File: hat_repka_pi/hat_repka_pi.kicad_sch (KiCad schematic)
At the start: 6 parts, among them J1 GPIO, U1 CAT24C256

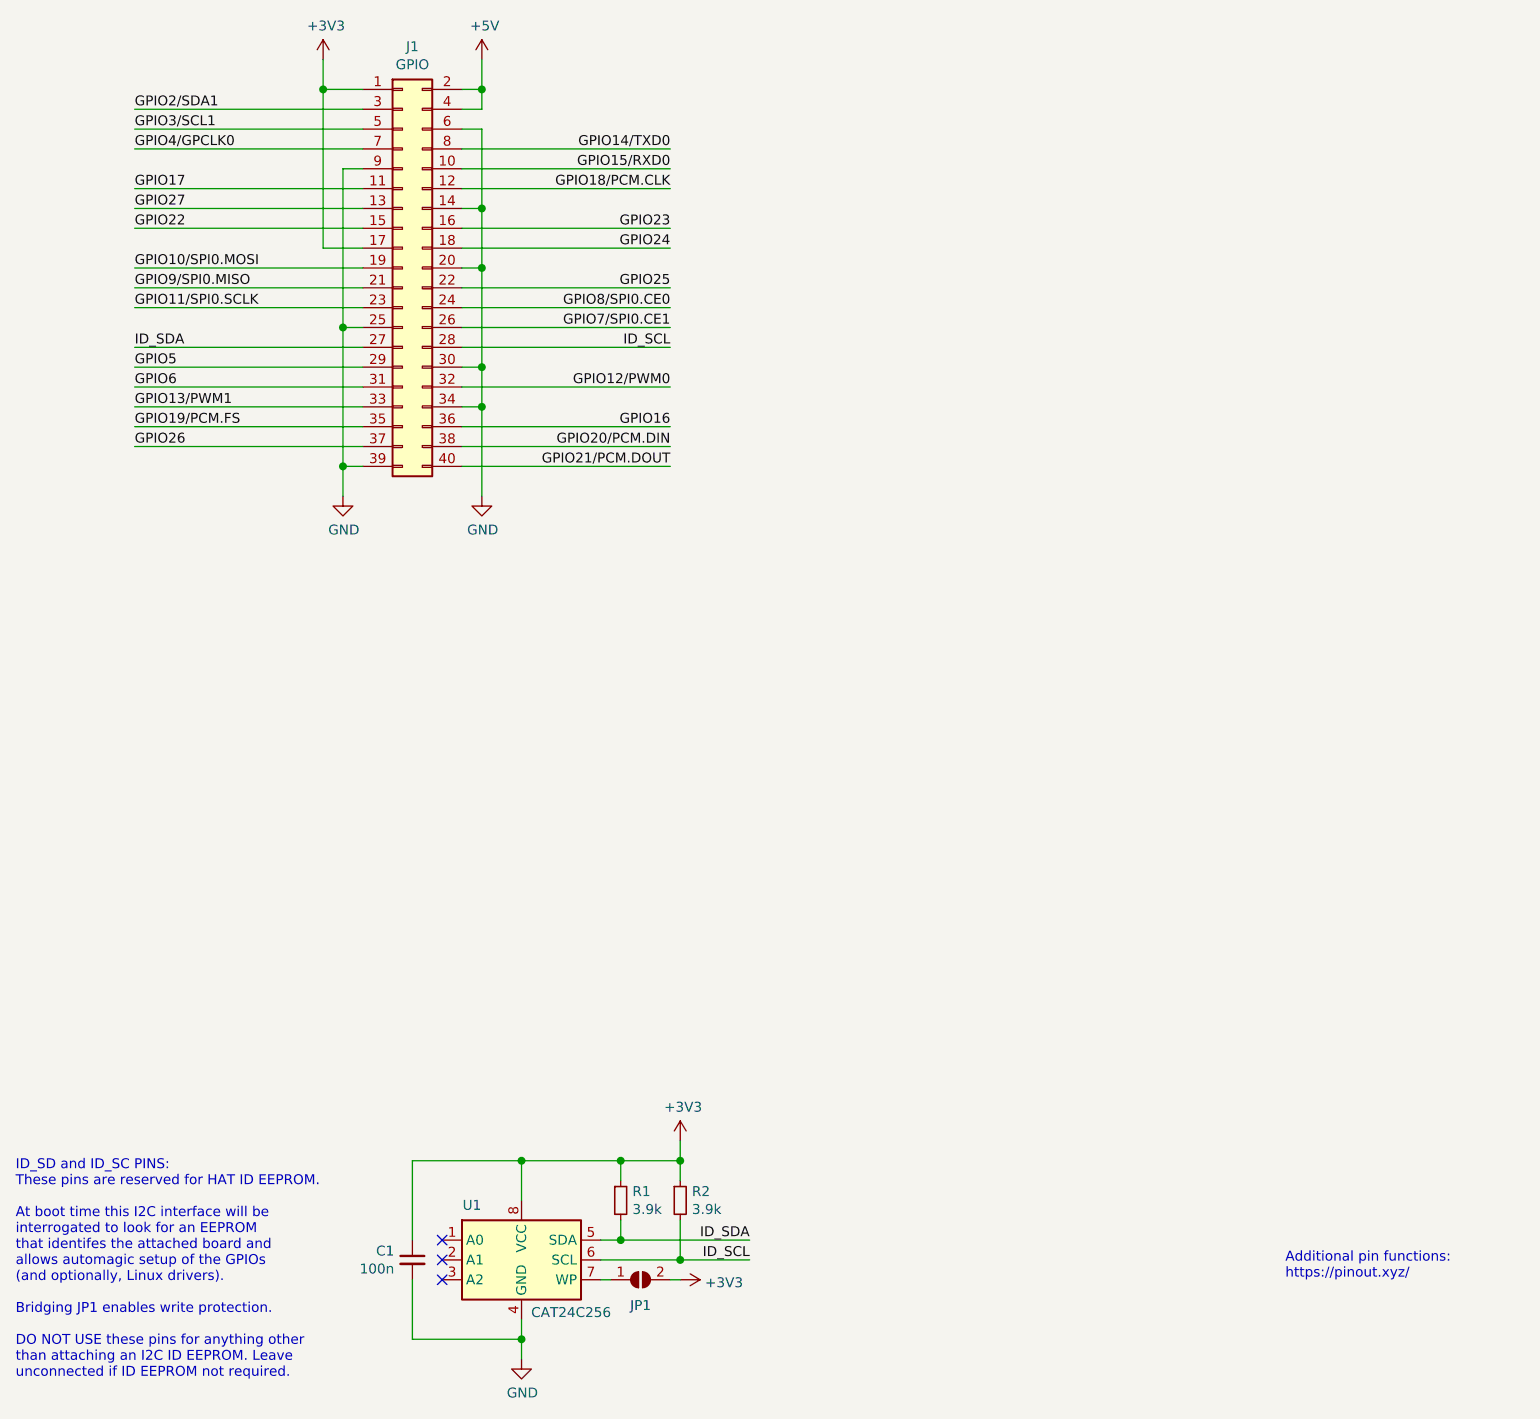
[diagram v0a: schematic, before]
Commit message: Добавлены файлы проекта шляпы для дисплея
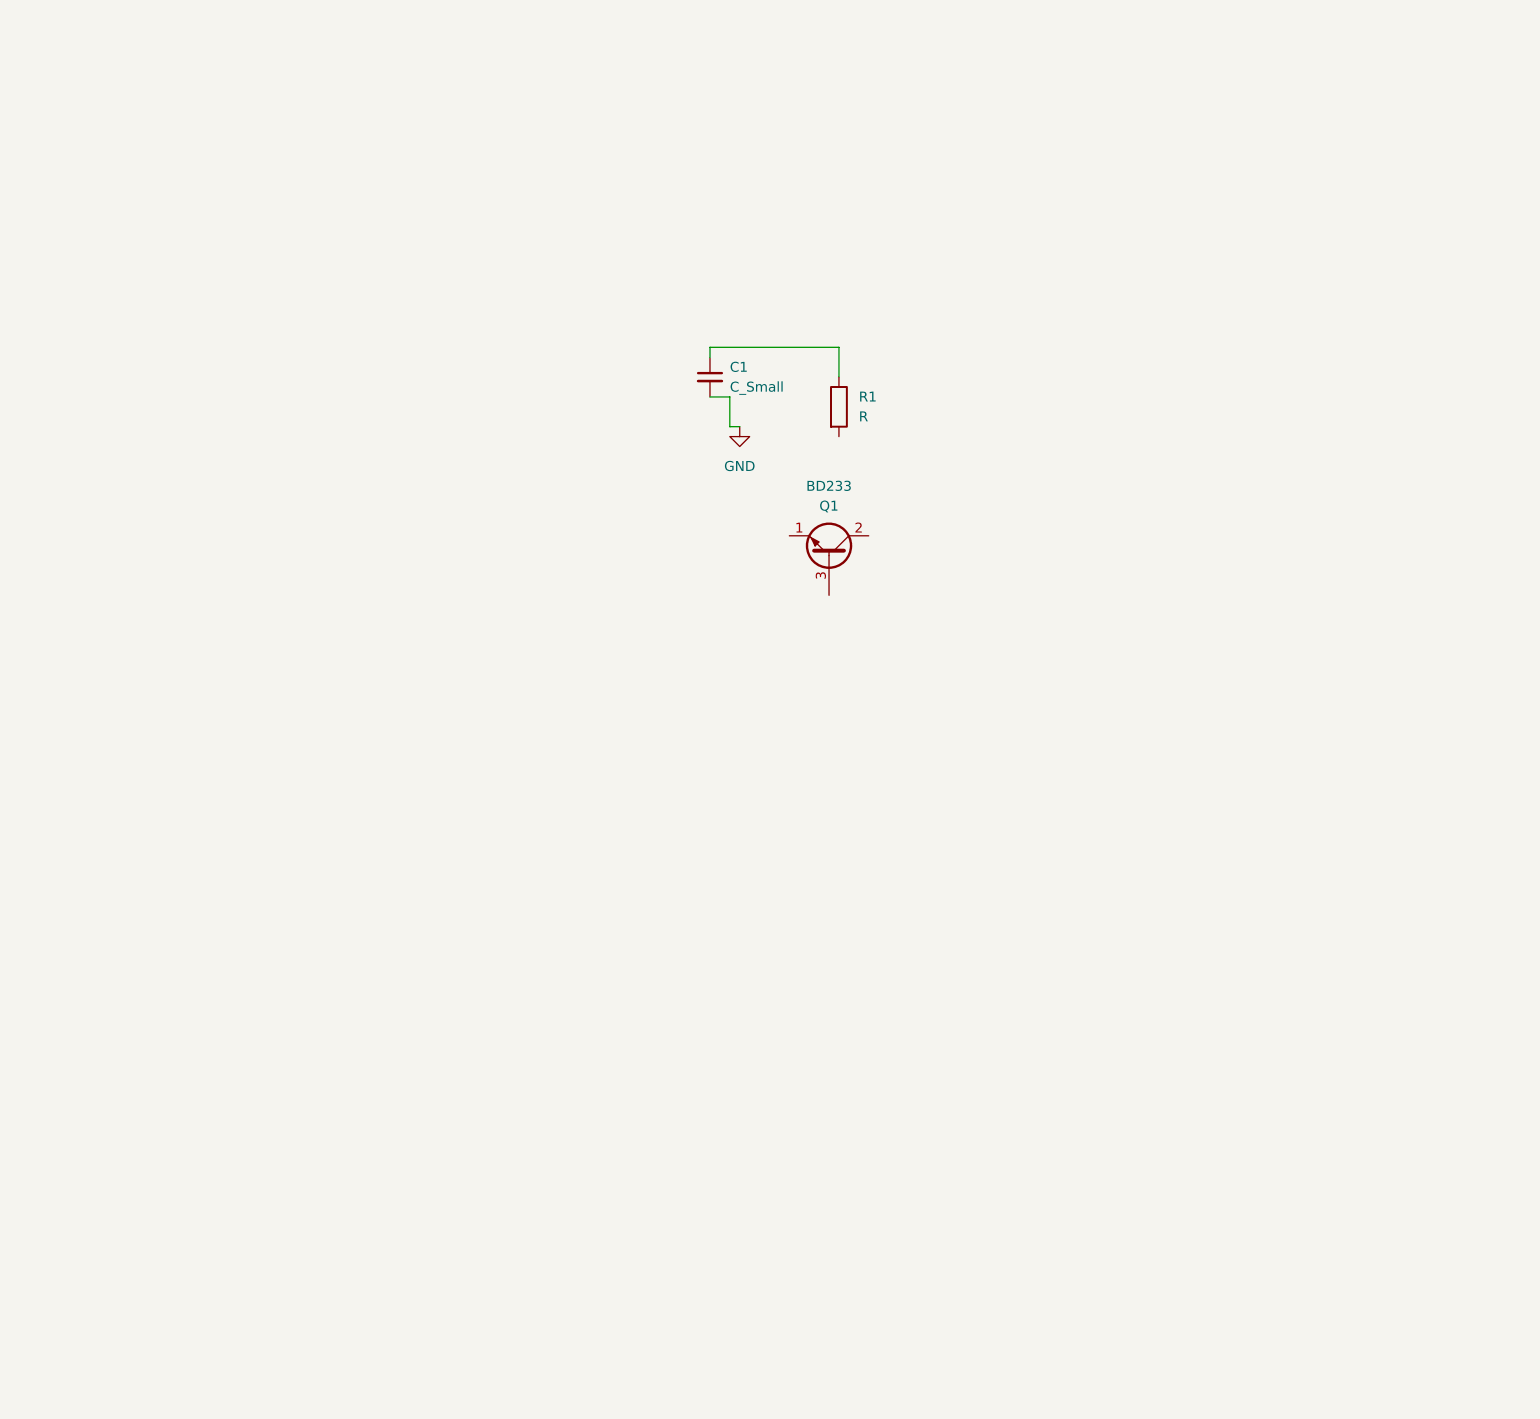
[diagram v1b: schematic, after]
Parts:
- removed J1: GPIO, Connector_PinSocket_2.54mm:PinSocket_2x20_P2.54mm_Vertical, symbol Connector_Generic:Conn_02x20_Odd_Even
- removed JP1: ID_WP, symbol Jumper:SolderJumper_2_Open
- removed R1, R2: 3.9k, symbol Device:R_Small
- removed U1: CAT24C256, symbol Memory_EEPROM:CAT24C256
- added Q1: BD233, Package_TO_SOT_THT:TO-126-3_Vertical, symbol Transistor_BJT:BD233
- added R1: R, symbol Device:R
- C1: value 100n -> C_Small
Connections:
- net +3V3: no longer names the net of C1.1
- net +3V3: now also R1.1
- no-connect marks 3 -> 0
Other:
- note removed: "Additional pin functions: https://pinout.xyz/"
- note removed: "ID_SD and ID_SC PINS: These pins are reserved for HAT ID EEPROM. At boot time this I2C interface will be interrogated to look for an EEPROM that identifes the attached board and allows automagic setup of the GPIOs (and optionally, Linux drivers). Bridging JP1 enables write protection. DO NOT USE these pins for anything other than attaching an I2C ID EEPROM. Leave unconnected if ID EEPROM not requ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"
